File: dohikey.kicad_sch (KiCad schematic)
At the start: 8 parts, among them J1 Conn_01x04_Pin, J2 DHT11, J3 Motor, J4 Barrel_Jack_Switch_Pin3Ring, Q1 PN2222A

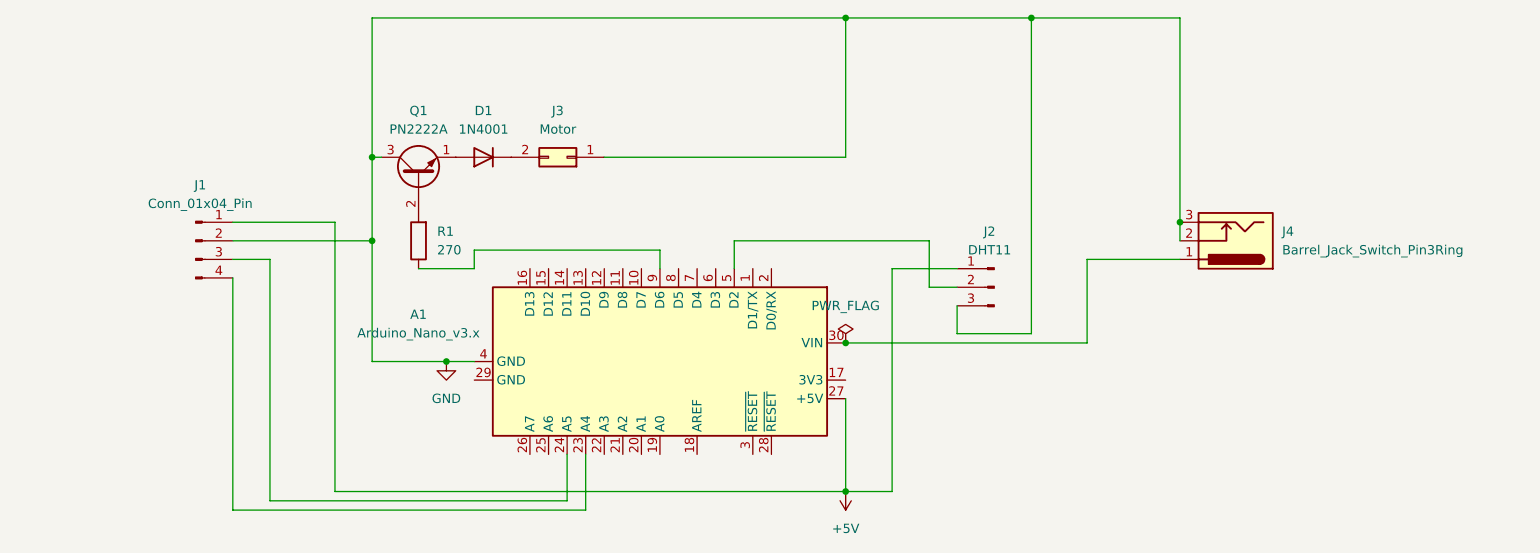
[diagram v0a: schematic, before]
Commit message: Add files via upload
Fixed LCD miswire. Data and Clock pins were swapped.
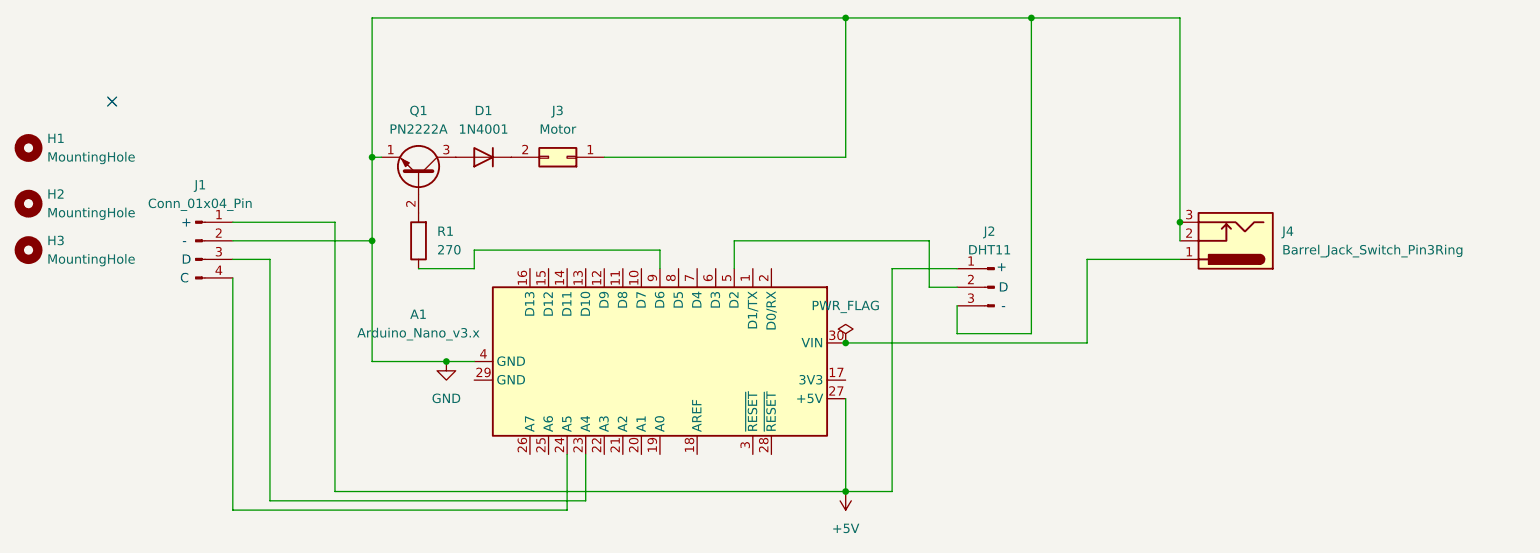
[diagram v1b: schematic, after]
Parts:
- added H1, H2, H3: MountingHole, MountingHole:MountingHole_2.2mm_M2, symbol Mechanical:MountingHole
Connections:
- net GND: now also Q1.1 (E); no longer Q1.3 (C)
- net at A1.23 (A4): now also J1.3 (Pin_3); no longer J1.4 (Pin_4)
- net at A1.24 (A5): now also J1.4 (Pin_4); no longer J1.3 (Pin_3)
- net at D1.2 (A): now also Q1.3 (C); no longer Q1.1 (E)
- no-connect marks 0 -> 1
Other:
- note added: "+"
- note added: "-"
- note added: "C"
- note added: "D"
- moved on the sheet: Q1
